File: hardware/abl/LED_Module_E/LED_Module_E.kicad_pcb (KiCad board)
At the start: 4 copper layers, 140.8 x 26 mm, 91 parts, among them J1 SFW20S-2STE1LF, J3 009159008603906, Q1 Si3456DDV, Q11 Si3456DDV, Q12 Si3456DDV, Q2 Si3456DDV, Q3 Si3456DDV, Q4 Si3456DDV, Q5 Si3456DDV, Q6 Si3456DDV, Q7 Si3456DDV, Q8 Si3456DDV, U1 TMP1075DGK, U2 74HC245, U3 24AA025UIDT-I/OT

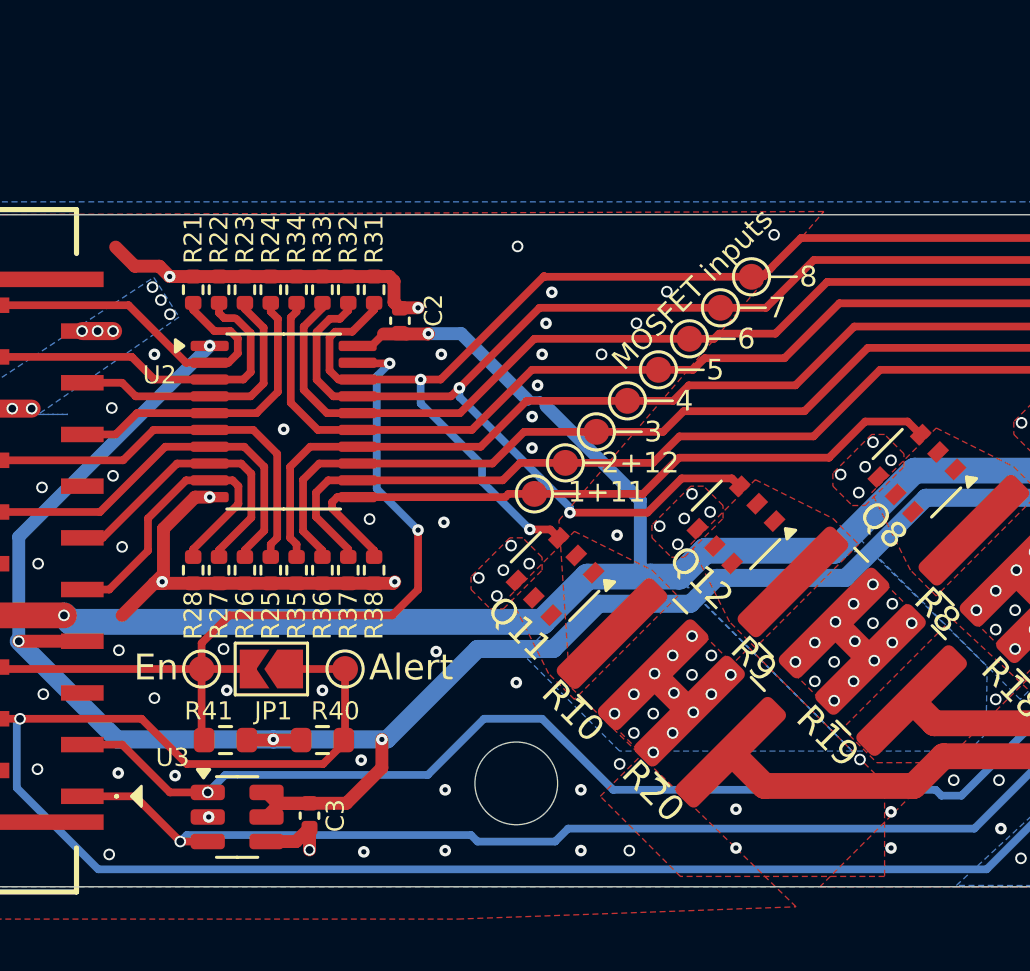
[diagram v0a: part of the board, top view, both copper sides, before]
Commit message: Fix reversed labeling of testpoints for mosfet inputs.
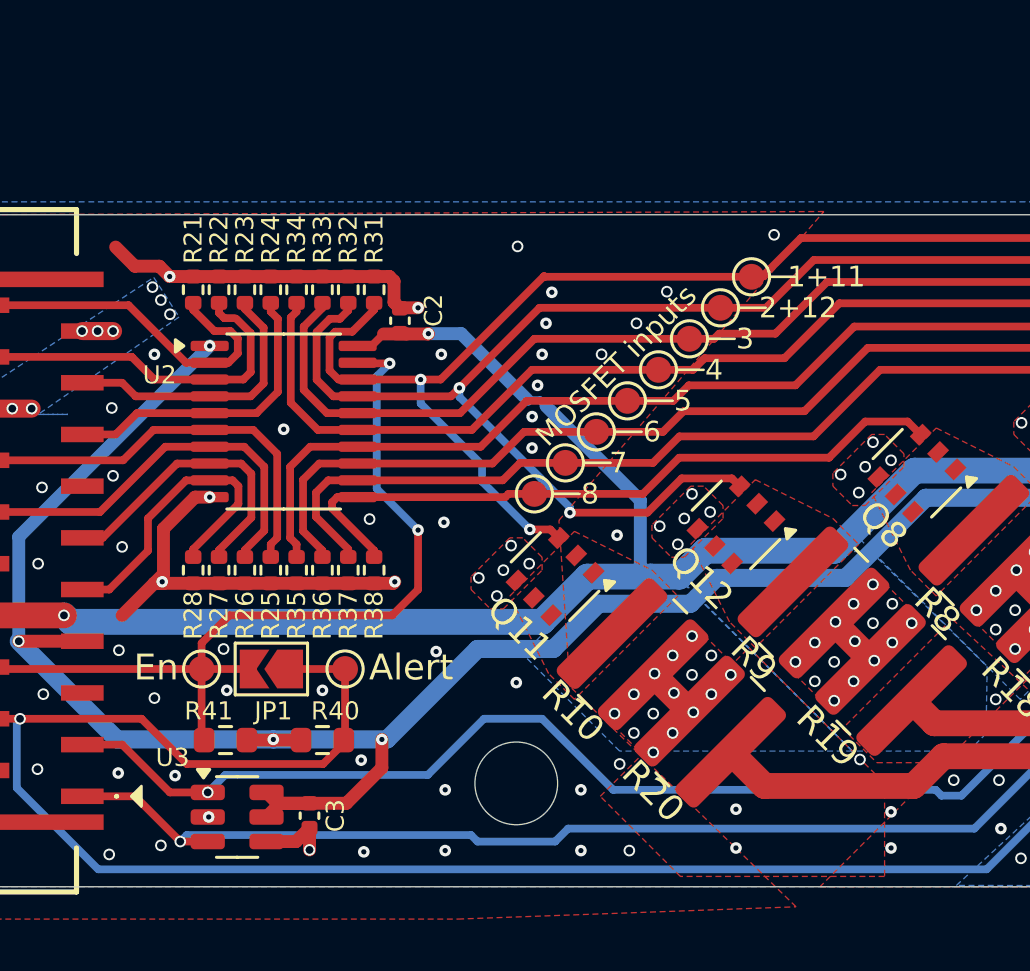
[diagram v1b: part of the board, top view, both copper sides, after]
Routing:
- net GND: vias 195 -> 196

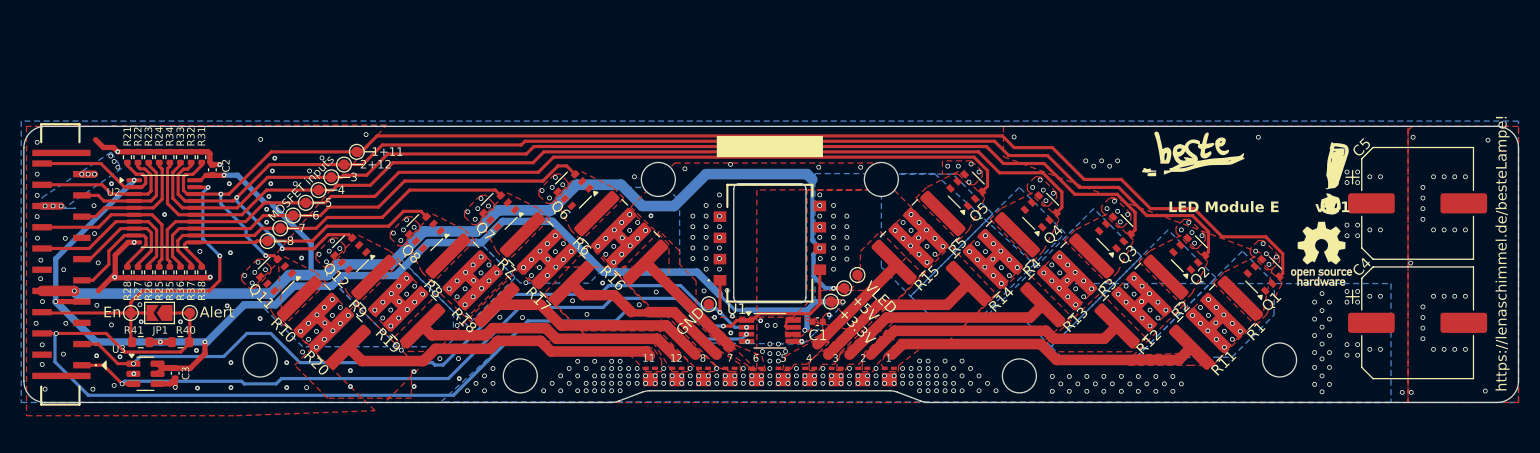
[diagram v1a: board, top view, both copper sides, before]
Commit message: Fix orientation of the flex connector.
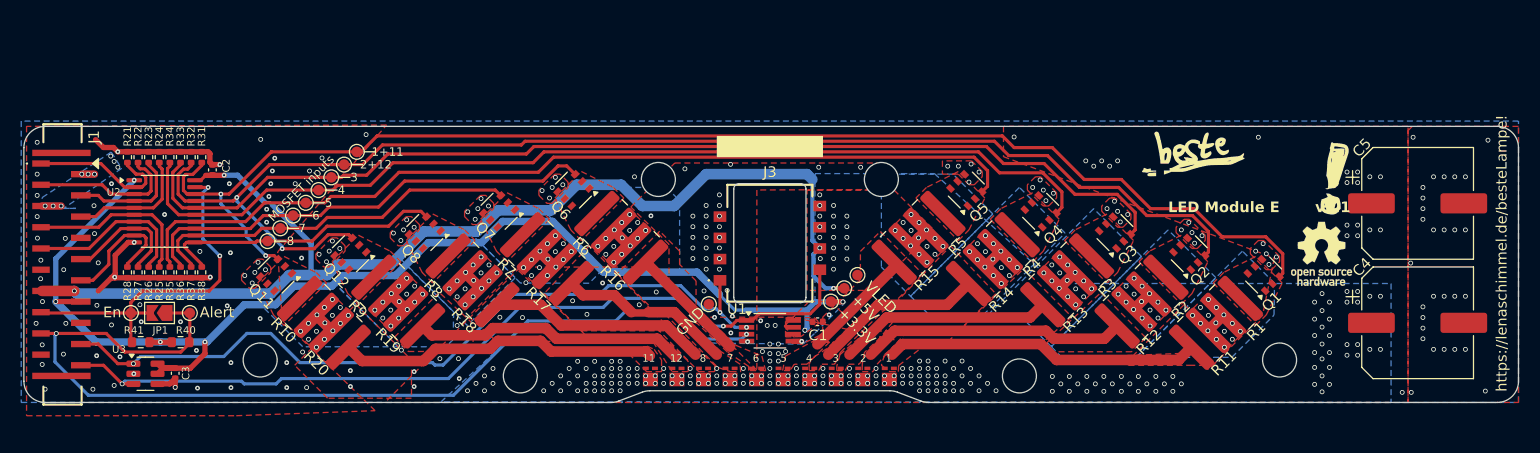
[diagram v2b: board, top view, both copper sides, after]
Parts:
- J1: footprint SFW20S-2STE1LF:SFW20S2STE1LF -> Own footprints:SFW20S2STE1LF_Own
- turned J1 to -90 degrees
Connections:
- J1 pad 1: /SDA -> /i1
- J1 pad 10: GND -> /i7
- J1 pad 11: /i7 -> GND
- J1 pad 12: /i6 -> /i8
- J1 pad 13: GND -> +5V
- J1 pad 14: /i5 -> +3.3V
- J1 pad 15: /i4 -> /ENABLE
- J1 pad 16: +4V -> GND
- J1 pad 17: /i3 -> /ALERT
- J1 pad 18: /i2 -> /SCL
- J1 pad 19: +4V -> GND
- J1 pad 2: GND -> +4V
- J1 pad 20: /i1 -> /SDA
- J1 pad 3: /SCL -> /i2
- J1 pad 4: /ALERT -> /i3
- J1 pad 5: GND -> +4V
- J1 pad 6: /ENABLE -> /i4
- J1 pad 7: +3.3V -> /i5
- J1 pad 8: +5V -> GND
- J1 pad 9: /i8 -> /i6

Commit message: Add small copper PCB that only contains LEDs and temperature sensor.
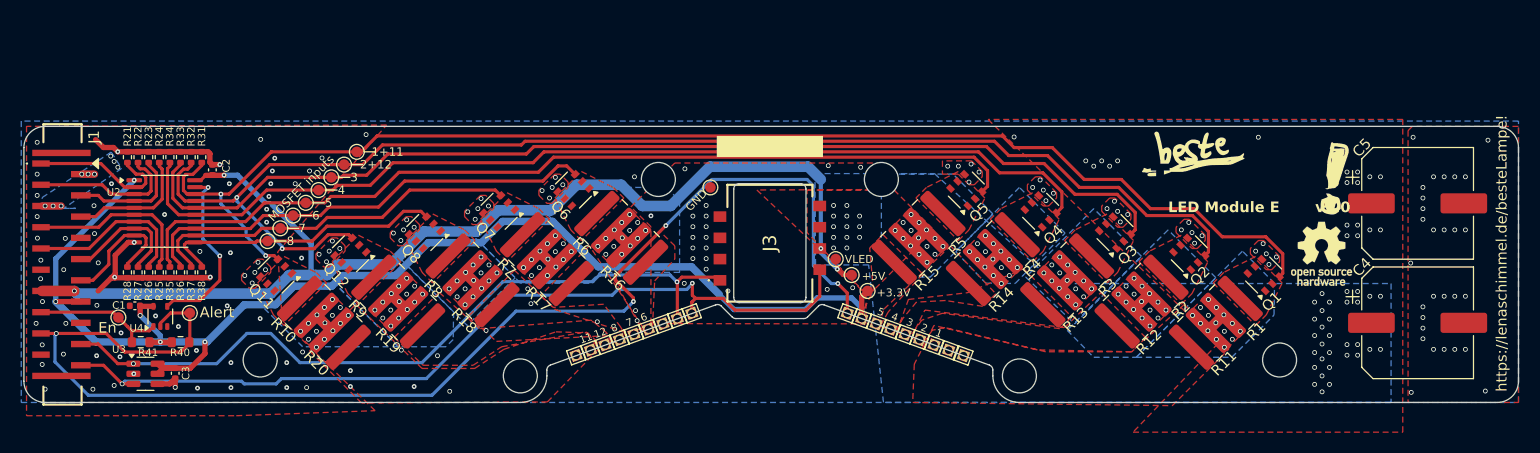
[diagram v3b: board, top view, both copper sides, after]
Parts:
- removed D1, D11, D12, D2, D3, D4, D5, D6, D7, D8: XEGAVT-H0-0000-000-000000K2001, Cree XLAMP XE-G LED XEGAVT-H0:XEGAVTH_clean
- removed JP1: SolderJumper_2_Open, Jumper:SolderJumper-2_P1.3mm_Open_TrianglePad1.0x1.5mm
- removed U1: TMP1075DGK, Package_SO:VSSOP-8_3.0x3.0mm_P0.65mm
- added K1: Conn_01x01, TestPoint:TestPoint_THTPad_1.0x1.0mm_Drill0.5mm, F.Cu at (119.2, 78.6)
- added K10: Conn_01x01, TestPoint:TestPoint_THTPad_1.0x1.0mm_Drill0.5mm, F.Cu at (144.8, 74.6)
- added K11: Conn_01x01, TestPoint:TestPoint_THTPad_1.0x1.0mm_Drill0.5mm, F.Cu at (146.2, 75.1)
- added K12: Conn_01x01, TestPoint:TestPoint_THTPad_1.0x1.0mm_Drill0.5mm, F.Cu at (147.5, 75.6)
- added K13: Conn_01x01, TestPoint:TestPoint_THTPad_1.0x1.0mm_Drill0.5mm, F.Cu at (148.9, 76.1)
- added K14: Conn_01x01, TestPoint:TestPoint_THTPad_1.0x1.0mm_Drill0.5mm, F.Cu at (150.2, 76.6)
- added K15: Conn_01x01, TestPoint:TestPoint_THTPad_1.0x1.0mm_Drill0.5mm, F.Cu at (151.6, 77.1)
- added K16: Conn_01x01, TestPoint:TestPoint_THTPad_1.0x1.0mm_Drill0.5mm, F.Cu at (153.0, 77.6)
- added K17: Conn_01x01, TestPoint:TestPoint_THTPad_1.0x1.0mm_Drill0.5mm, F.Cu at (154.3, 78.1)
- added K18: Conn_01x01, TestPoint:TestPoint_THTPad_1.0x1.0mm_Drill0.5mm, F.Cu at (155.7, 78.6)
- added K2: Conn_01x01, TestPoint:TestPoint_THTPad_1.0x1.0mm_Drill0.5mm, F.Cu at (120.6, 78.1)
- added K3: Conn_01x01, TestPoint:TestPoint_THTPad_1.0x1.0mm_Drill0.5mm, F.Cu at (122.0, 77.6)
- added K4: Conn_01x01, TestPoint:TestPoint_THTPad_1.0x1.0mm_Drill0.5mm, F.Cu at (123.3, 77.1)
- added K5: Conn_01x01, TestPoint:TestPoint_THTPad_1.0x1.0mm_Drill0.5mm, F.Cu at (124.7, 76.6)
- added K6: Conn_01x01, TestPoint:TestPoint_THTPad_1.0x1.0mm_Drill0.5mm, F.Cu at (126.1, 76.1)
- added K7: Conn_01x01, TestPoint:TestPoint_THTPad_1.0x1.0mm_Drill0.5mm, F.Cu at (127.4, 75.6)
- added K8: Conn_01x01, TestPoint:TestPoint_THTPad_1.0x1.0mm_Drill0.5mm, F.Cu at (128.8, 75.1)
- added K9: Conn_01x01, TestPoint:TestPoint_THTPad_1.0x1.0mm_Drill0.5mm, F.Cu at (130.2, 74.6)
- added U4: 74LVC1G32, Package_TO_SOT_SMD:SOT-353_SC-70-5, F.Cu at (80.1, 74.9)
- J3: footprint 009159008603906:009159008603906 -> Own footprints:Dual Row Inverted Thru Board Card Edge Connector 02x04 Kyocera AVX 009159008603906
- moved C1 64.3 mm to (77.7, 73.9), turned to 0 degrees
- moved TP1 11.0 mm to (131.9, 62.8)
- moved TP2 3.59 mm to (146.7, 72.5)
- moved TP3 2.54 mm to (143.7, 69.5)
- moved TP4 1.43 mm to (145.2, 71.0)
- moved TP6 1.25 mm to (76.2, 75.0)
- turned R41 to 180 degrees
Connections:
- R41 pad 1: /ENABLE -> +3.3V
- R41 pad 2: +3.3V -> /ENABLE
- U2 pad 19: /ENABLE -> Net-(U2-CE)
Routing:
- net Net-(K2-Pin_1): track 30.3 -> 0.00 mm
- net Net-(K16-Pin_1): track 29.7 -> 0.00 mm
- net /ALERT: track 93.8 -> 123.0 mm, vias 2 -> 4
- net Net-(K3-Pin_1): track 25.6 -> 0.00 mm
- net Net-(K15-Pin_1): track 24.9 -> 0.00 mm
- net /ENABLE: track 34.2 -> 13.1 mm, vias 2 -> 0
- net Net-(K4-Pin_1): track 20.7 -> 0.00 mm
- net Net-(K14-Pin_1): track 20.2 -> 0.00 mm
- net Net-(U2-CE): track 0.00 -> 16.8 mm, vias 0 -> 2
- net Net-(K5-Pin_1): track 16.5 -> 0.00 mm
- net Net-(K13-Pin_1): track 16.0 -> 0.00 mm
- net Net-(K6-Pin_1): track 11.2 -> 0.00 mm
- net Net-(K12-Pin_1): track 10.7 -> 0.00 mm
- net /SCL: track 73.6 -> 70.6 mm, vias 3 -> 2
- net +3.3V: track 124.9 -> 123.0 mm, vias 6 -> 5
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- removed copper zone on F.Cu, net +3.3V
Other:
- outline, holes or cut-outs redrawn
- board text added: "LED Module E v3.0"
- board text removed: "LED Module E v2.1"

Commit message: Many, many minor updates to the big PCBs, and a few simple helper PCBs.
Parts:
- C4, C5: value 680uF -> 1000uF
- U3: value 24AA025UIDT-I/OT -> 24AA025E48T-I/OT
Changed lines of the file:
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@@
 			)
 		)
-		(property "Value" "680uF"
+		(property "Value" "1000uF"
 			(at 0 6.2 0)
 			(layer "F.Fab")
@@
 		(sheetname "Root")
 		(sheetfile "LED_Module_E.kicad_sch")
-		(attr exclude_from_pos_files)
+		(attr exclude_from_pos_files dnp)
 		(fp_line
 			(start -0.7 0.7)
@@
 		(sheetname "Root")
 		(sheetfile "LED_Module_E.kicad_sch")
-		(attr exclude_from_pos_files exclude_from_bom)
+		(attr exclude_from_pos_files exclude_from_bom dnp)
 		(fp_circle
 			(center 0 0)
@@
 		(sheetname "Root")
 		(sheetfile "LED_Module_E.kicad_sch")
-		(attr exclude_from_pos_files)
+		(attr exclude_from_pos_files dnp)
 		(fp_circle
 			(center 0 0)
@@
 		(sheetname "Root")
 		(sheetfile "LED_Module_E.kicad_sch")
-		(attr exclude_from_pos_files)
+		(attr exclude_from_pos_files dnp)
 		(fp_circle
 			(center 0 0)
@@
 		(sheetname "Root")
 		(sheetfile "LED_Module_E.kicad_sch")
-		(attr exclude_from_pos_files)
+		(attr exclude_from_pos_files dnp)
 		(fp_line
 			(start -0.7 -0.7)
@@
 		(sheetname "Root")
 		(sheetfile "LED_Module_E.kicad_sch")
-		(attr exclude_from_pos_files)
+		(attr exclude_from_pos_files dnp)
 		(fp_circle
 			(center 0 0)
@@
 		(sheetname "Root")
 		(sheetfile "LED_Module_E.kicad_sch")
-		(attr exclude_from_pos_files)
+		(attr exclude_from_pos_files dnp)
 		(fp_line
 			(start -0.7 0.7)
@@
 		(sheetname "Root")
 		(sheetfile "LED_Module_E.kicad_sch")
-		(attr exclude_from_pos_files)
+		(attr exclude_from_pos_files dnp)
 		(fp_circle
 			(center 0 0)
@@
 		(sheetname "Root")
 		(sheetfile "LED_Module_E.kicad_sch")
-		(attr exclude_from_pos_files)
+		(attr exclude_from_pos_files dnp)
 		(fp_line
 			(start -0.7 -0.7)
@@
 		(sheetname "Root")
 		(sheetfile "LED_Module_E.kicad_sch")
-		(attr exclude_from_pos_files)
+		(attr exclude_from_pos_files dnp)
 		(fp_circle
 			(center 0 0)
@@
 		(sheetname "Root")
 		(sheetfile "LED_Module_E.kicad_sch")
-		(attr exclude_from_pos_files)
+		(attr exclude_from_pos_files dnp)
 		(fp_line
 			(start -0.7 -0.7)
@@
 		(sheetname "Root")
 		(sheetfile "LED_Module_E.kicad_sch")
-		(attr exclude_from_pos_files)
+		(attr exclude_from_pos_files dnp)
 		(fp_circle
 			(center 0 0)
@@
 		(sheetname "Root")
 		(sheetfile "LED_Module_E.kicad_sch")
-		(attr exclude_from_pos_files)
+		(attr exclude_from_pos_files dnp)
 		(fp_line
 			(start -0.7 0.7)
@@
 		(sheetname "Root")
 		(sheetfile "LED_Module_E.kicad_sch")
-		(attr exclude_from_pos_files)
+		(attr exclude_from_pos_files dnp)
 		(fp_circle
 			(center 0 0)
@@
 		(sheetname "Root")
 		(sheetfile "LED_Module_E.kicad_sch")
-		(attr exclude_from_pos_files exclude_from_bom)
+		(attr exclude_from_pos_files exclude_from_bom dnp)
 		(fp_circle
 			(center 0 0)
@@
 		(sheetname "Root")
 		(sheetfile "LED_Module_E.kicad_sch")
-		(attr exclude_from_pos_files)
+		(attr exclude_from_pos_files dnp)
 		(fp_line
 			(start -0.7 0.7)
@@
 		(sheetname "Root")
 		(sheetfile "LED_Module_E.kicad_sch")
-		(attr exclude_from_pos_files)
+		(attr exclude_from_pos_files dnp)
 		(fp_line
 			(start -0.7 -0.7)
@@
 		(sheetname "Root")
 		(sheetfile "LED_Module_E.kicad_sch")
-		(attr exclude_from_pos_files)
+		(attr exclude_from_pos_files dnp)
 		(fp_line
 			(start -0.7 0.7)
@@
 			)
 		)
-		(property "Value" "24AA025UIDT-I/OT"
+		(property "Value" "24AA025E48T-I/OT"
 			(at 0 2.4 0)
 			(layer "F.Fab")
@@
 			)
 		)
-		(property "Datasheet" "http://ww1.microchip.com/downloads/en/DeviceDoc/21709J.pdf"
+		(property "Datasheet" "https://www.lcsc.com/datasheet/lcsc_datasheet_1810121540_Microchip-Tech-24AA025E48T-I-OT_C129895.pdf"
 			(at 0 0 0)
 			(unlocked yes)
@@
 			)
 		)
-		(property "Manufacturer_Part_Number" "24AA025UIDT-I/OT"
+		(property "Manufacturer_Part_Number" "24AA025E48T-I/OT"
 			(at 0 0 0)
 			(unlocked yes)
@@
 			)
 		)
-		(property "LCSC Part #" "C2061498"
+		(property "LCSC Part #" "C129895"
 			(at 0 0 0)
 			(unlocked yes)
@@
 			)
 		)
+		(property "LCSC Part #" "C460530"
+			(at 0 0 90)
+			(unlocked yes)
+			(layer "F.Fab")
+			(hide yes)
+			(effects
+				(font
+					(size 1 1)
+					(thickness 0.15)
+				)
+			)
+		)
+		(property "Manufacturer_Part_Number" "74LVC1G32SE"
+			(at 0 0 90)
+			(unlocked yes)
+			(layer "F.Fab")
+			(hide yes)
+			(effects
+				(font
+					(size 1 1)
+					(thickness 0.15)
+				)
+			)
+		)
 		(property ki_fp_filters "SOT* SG-*")
 		(sheetname "Root")
@@
 		)
 		(fp_text user "${REFERENCE}"
-			(at 0 0 360)
+			(at 0 0 0)
 			(layer "F.Fab")
 			(effects
@@
 		(sheetname "Root")
 		(sheetfile "LED_Module_E.kicad_sch")
-		(attr exclude_from_pos_files)
+		(attr exclude_from_pos_files dnp)
 		(fp_line
 			(start -0.7 -0.7)
@@
 		(sheetname "Root")
 		(sheetfile "LED_Module_E.kicad_sch")
-		(attr exclude_from_pos_files exclude_from_bom)
+		(attr exclude_from_pos_files exclude_from_bom dnp)
 		(fp_poly
 			(pts
@@
 		(sheetname "Root")
 		(sheetfile "LED_Module_E.kicad_sch")
-		(attr exclude_from_pos_files exclude_from_bom)
+		(attr exclude_from_pos_files exclude_from_bom dnp)
 		(fp_circle
 			(center 0 0)
@@
 		(sheetname "Root")
 		(sheetfile "LED_Module_E.kicad_sch")
-		(attr exclude_from_pos_files)
+		(attr exclude_from_pos_files dnp)
 		(fp_circle
 			(center 0 0)
@@
 		(sheetname "Root")
 		(sheetfile "LED_Module_E.kicad_sch")
-		(attr exclude_from_pos_files)
+		(attr exclude_from_pos_files dnp)
 		(fp_line
 			(start -0.7 -0.7)
@@
 		(sheetname "Root")
 		(sheetfile "LED_Module_E.kicad_sch")
-		(attr exclude_from_pos_files)
+		(attr exclude_from_pos_files dnp)
 		(fp_line
 			(start -0.7 -0.7)
@@
 			)
 		)
-		(property "Value" "680uF"
+		(property "Value" "1000uF"
 			(at 0 6.2 0)
 			(layer "F.Fab")
@@
 			)
 		)
-		(property "Manufacturer_Part_Number" "RVT1A681M0810 680UF 10V"
+		(property "Manufacturer_Part_Number" "VKME1301C102MV"
 			(at 0 0 0)
 			(unlocked yes)
@@
 			)
 		)
-		(property "LCSC Part #" "C2760485"
+		(property "LCSC Part #" "C487313"
 			(at 0 0 0)
 			(unlocked yes)
@@
 		(sheetname "Root")
 		(sheetfile "LED_Module_E.kicad_sch")
-		(attr exclude_from_pos_files exclude_from_bom)
+		(attr exclude_from_pos_files exclude_from_bom dnp)
 		(fp_circle
 			(center 0 0)
@@
 		(sheetname "Root")
 		(sheetfile "LED_Module_E.kicad_sch")
-		(attr exclude_from_pos_files)
+		(attr exclude_from_pos_files dnp)
 		(fp_circle
 			(center 0 0)
@@
 		(sheetname "Root")
 		(sheetfile "LED_Module_E.kicad_sch")
-		(attr exclude_from_pos_files exclude_from_bom)
+		(attr exclude_from_pos_files exclude_from_bom dnp)
 		(fp_circle
 			(center 0 0)
@@
 		(sheetname "Root")
 		(sheetfile "LED_Module_E.kicad_sch")
-		(attr exclude_from_pos_files)
+		(attr exclude_from_pos_files dnp)
 		(fp_circle
 			(center 0 0)
@@
 		(sheetname "Root")
 		(sheetfile "LED_Module_E.kicad_sch")
-		(attr exclude_from_pos_files)
+		(attr exclude_from_pos_files dnp)
 		(fp_circle
 			(center 0 0)
@@
 		(sheetname "Root")
 		(sheetfile "LED_Module_E.kicad_sch")
-		(attr exclude_from_pos_files)
+		(attr exclude_from_pos_files dnp)
 		(fp_line
 			(start -0.7 0.7)
@@
 		(sheetname "Root")
 		(sheetfile "LED_Module_E.kicad_sch")
-		(attr exclude_from_pos_files)
+		(attr exclude_from_pos_files dnp)
 		(fp_circle
 			(center 0 0)
@@
 		(sheetname "Root")
 		(sheetfile "LED_Module_E.kicad_sch")
-		(attr exclude_from_pos_files)
+		(attr exclude_from_pos_files dnp)
 		(fp_circle
 			(center 0 0)
@@
 		(tags "capacitor")
 		(property "Reference" "C1"
-			(at -1.5 -0.05 360)
+			(at -1.5 -0.05 0)
 			(layer "F.SilkS")
 			(effects
@@
 		)
 		(property "Value" "100nF"
-			(at 0 1.16 360)
+			(at 0 1.16 0)
 			(layer "F.Fab")
 			(effects
@@
 		)
 		(fp_text user "${REFERENCE}"
-			(at 0 0 360)
+			(at 0 0 0)
 			(layer "F.Fab")
 			(effects
@@
 		(sheetname "Root")
 		(sheetfile "LED_Module_E.kicad_sch")
-		(attr exclude_from_pos_files)
+		(attr exclude_from_pos_files dnp)
 		(fp_line
 			(start -0.7 0.7)
@@
 		(sheetname "Root")
 		(sheetfile "LED_Module_E.kicad_sch")
-		(attr exclude_from_pos_files)
+		(attr exclude_from_pos_files dnp)
 		(fp_line
 			(start -0.7 -0.7)
@@
 		(sheetname "Root")
 		(sheetfile "LED_Module_E.kicad_sch")
-		(attr exclude_from_pos_files exclude_from_bom)
+		(attr exclude_from_pos_files exclude_from_bom dnp)
 		(fp_circle
 			(center 0 0)
@@
 		(sheetname "Root")
 		(sheetfile "LED_Module_E.kicad_sch")
-		(attr exclude_from_pos_files)
+		(attr exclude_from_pos_files dnp)
 		(fp_line
 			(start -0.7 -0.7)
@@
 		(sheetname "Root")
 		(sheetfile "LED_Module_E.kicad_sch")
-		(attr exclude_from_pos_files)
+		(attr exclude_from_pos_files dnp)
 		(fp_circle
 			(center 0 0)
@@
 		(sheetname "Root")
 		(sheetfile "LED_Module_E.kicad_sch")
-		(attr exclude_from_pos_files)
+		(attr exclude_from_pos_files dnp)
 		(fp_line
 			(start -0.7 0.7)
@@
 		(sheetname "Root")
 		(sheetfile "LED_Module_E.kicad_sch")
-		(attr exclude_from_pos_files)
+		(attr exclude_from_pos_files dnp)
 		(fp_line
 			(start -0.7 0.7)
